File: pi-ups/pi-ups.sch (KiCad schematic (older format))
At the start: 34 parts, among them J1 , Q1 IRLML2244, Q2 IRLML2244, Q3 IRLML2244, Q4 IRLML2244, U1 BMS_1S, U2 DC-DC, U3 BMS_1S, U4 FTDI232, U5 Arduino_Pro_Mini

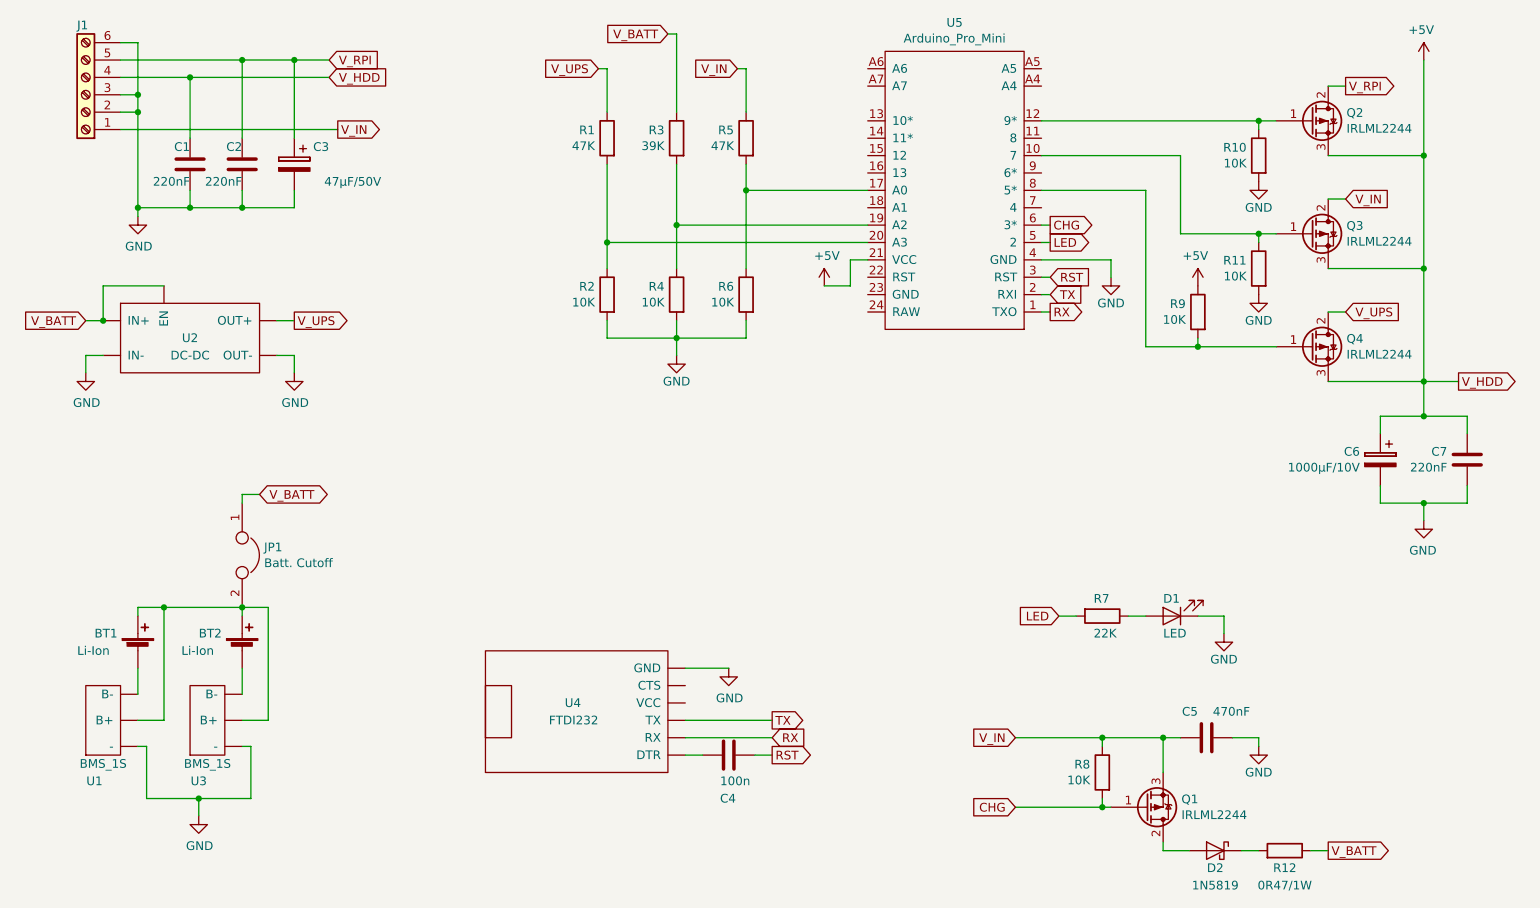
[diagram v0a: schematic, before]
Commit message: Update pi-ups.sch
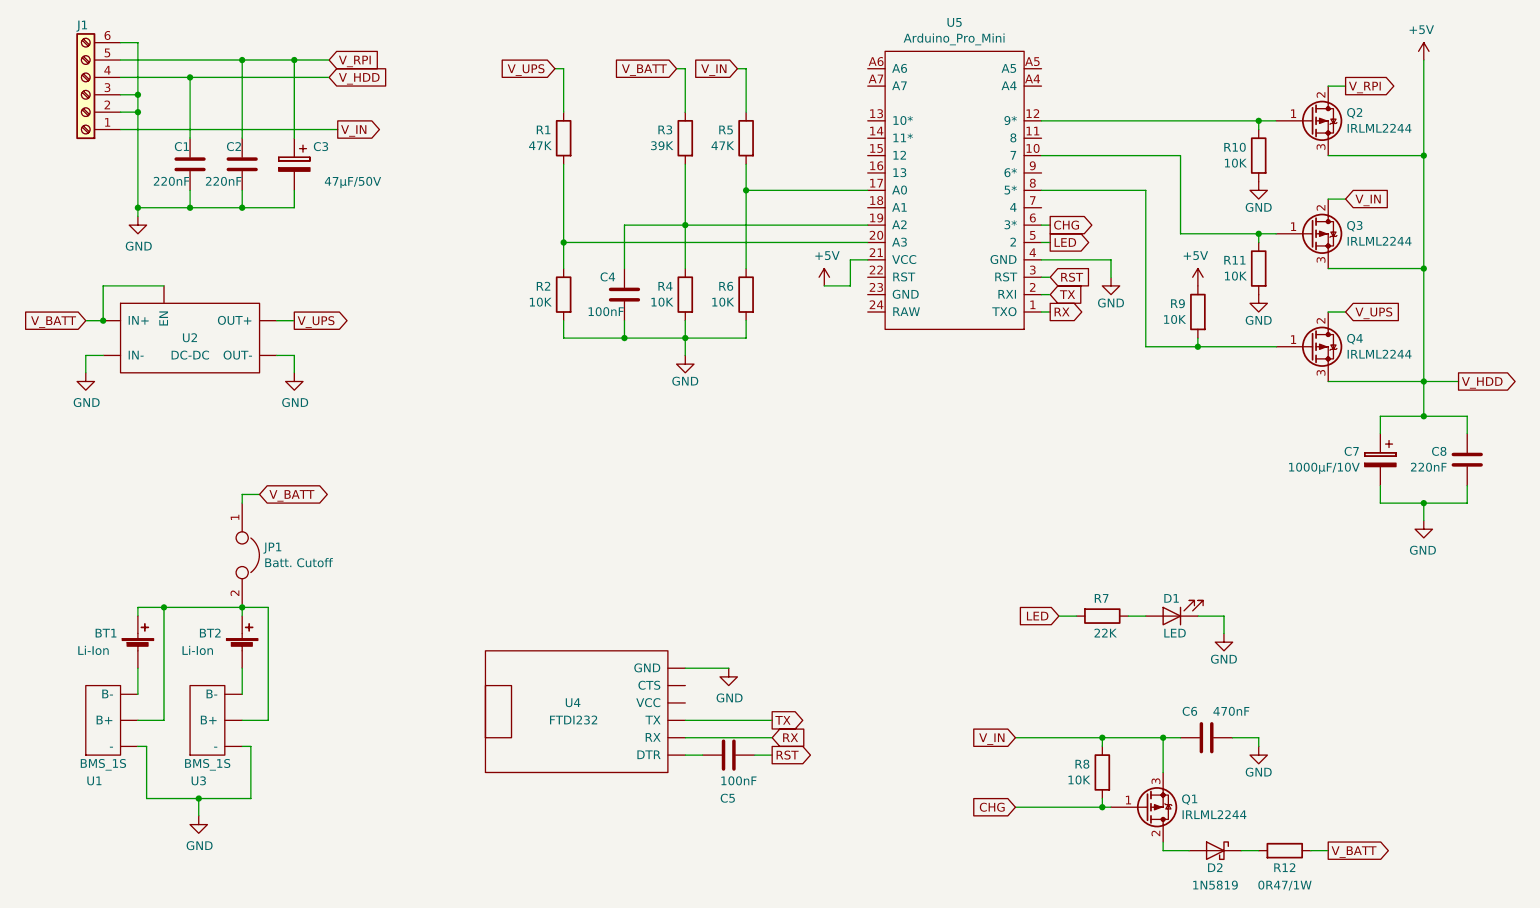
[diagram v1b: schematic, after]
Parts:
- added C4: 100nF, symbol Device:C
- C5: renamed from C4; value 100n -> 100nF
- renumbered C5 to C6, C6 to C7, C7 to C8
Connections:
- net GND: now also C4.2
- net at R3.2, R4.1, U5.19 (A2): now also C4.1
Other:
- moved on the sheet: R1, R2, R3, R4
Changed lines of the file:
@@
 $EndComp
 $Comp
-L Device:C C4
+L Device:C C5
 U 1 1 5CDDD4BF
 P 5700 5350
-F 0 "C4" V 5950 5400 50  0000 R CNN
-F 1 "100n" V 5850 5400 50  0000 R CNN
+F 0 "C5" V 5950 5400 50  0000 R CNN
+F 1 "100nF" V 5850 5400 50  0000 R CNN
 F 2 "" H 5738 5200 50  0001 C CNN
 F 3 "~" H 5700 5350 50  0001 C CNN
@@
 $EndComp
 $Comp
-L Device:CP C6
+L Device:CP C7
 U 1 1 5CE05AE7
 P 9450 3650
-F 0 "C6" H 9568 3696 50  0000 L CNN
+F 0 "C7" H 9568 3696 50  0000 L CNN
 F 1 "1000µF/10V" H 9568 3605 50  0000 L CNN
 F 2 "" H 9488 3500 50  0001 C CNN
@@
 $EndComp
 $Comp
-L Device:C C7
+L Device:C C8
 U 1 1 5CE05C0B
 P 9950 3650
-F 0 "C7" H 9835 3696 50  0000 R CNN
+F 0 "C8" H 9835 3696 50  0000 R CNN
 F 1 "220nF" H 9835 3605 50  0000 R CNN
 F 2 "" H 9988 3500 50  0001 C CNN
@@
 L Device:R R4
 U 1 1 5CE7E21F
-P 5400 2700
-F 0 "R4" H 5470 2746 50  0000 L CNN
-F 1 "10K" H 5470 2655 50  0000 L CNN
-F 2 "" V 5330 2700 50  0001 C CNN
-F 3 "~" H 5400 2700 50  0001 C CNN
-	1    5400 2700
+P 5450 2700
+F 0 "R4" H 5520 2746 50  0000 L CNN
+F 1 "10K" H 5520 2655 50  0000 L CNN
+F 2 "" V 5380 2700 50  0001 C CNN
+F 3 "~" H 5450 2700 50  0001 C CNN
+	1    5450 2700
 	-1   0    0    -1
 $EndComp
@@
 L Device:R R2
 U 1 1 5CE7E25D
-P 5000 2700
-F 0 "R2" H 5070 2746 50  0000 L CNN
-F 1 "10K" H 5070 2655 50  0000 L CNN
-F 2 "" V 4930 2700 50  0001 C CNN
-F 3 "~" H 5000 2700 50  0001 C CNN
-	1    5000 2700
+P 4750 2700
+F 0 "R2" H 4820 2746 50  0000 L CNN
+F 1 "10K" H 4820 2655 50  0000 L CNN
+F 2 "" V 4680 2700 50  0001 C CNN
+F 3 "~" H 4750 2700 50  0001 C CNN
+	1    4750 2700
 	-1   0    0    -1
 $EndComp
@@
 	5800 2850 5800 2950
 Wire Wire Line
-	5800 2950 5400 2950
-Wire Wire Line
-	5000 2950 5000 2850
+	4750 2950 4750 2850
 $Comp
 L power:GND #PWR05
 U 1 1 5CE8025B
-P 5400 3050
-F 0 "#PWR05" H 5400 2800 50  0001 C CNN
-F 1 "GND" H 5400 2900 50  0000 C CNN
-F 2 "" H 5400 3050 50  0001 C CNN
-F 3 "" H 5400 3050 50  0001 C CNN
-	1    5400 3050
-	-1   0    0    -1
-$EndComp
-Wire Wire Line
-	5400 3050 5400 2950
-Connection ~ 5400 2950
-Wire Wire Line
-	5400 2950 5000 2950
-Wire Wire Line
-	5400 2850 5400 2950
+P 5450 3050
+F 0 "#PWR05" H 5450 2800 50  0001 C CNN
+F 1 "GND" H 5450 2900 50  0000 C CNN
+F 2 "" H 5450 3050 50  0001 C CNN
+F 3 "" H 5450 3050 50  0001 C CNN
+	1    5450 3050
+	-1   0    0    -1
+$EndComp
+Wire Wire Line
+	5450 3050 5450 2950
+Connection ~ 5450 2950
+Wire Wire Line
+	5450 2950 5100 2950
+Wire Wire Line
+	5450 2850 5450 2950
 $Comp
 L Device:R R5
@@
 L Device:R R3
 U 1 1 5CE8442D
-P 5400 1800
-F 0 "R3" H 5470 1846 50  0000 L CNN
-F 1 "39K" H 5470 1755 50  0000 L CNN
-F 2 "" V 5330 1800 50  0001 C CNN
-F 3 "~" H 5400 1800 50  0001 C CNN
-	1    5400 1800
+P 5450 1800
+F 0 "R3" H 5520 1846 50  0000 L CNN
+F 1 "39K" H 5520 1755 50  0000 L CNN
+F 2 "" V 5380 1800 50  0001 C CNN
+F 3 "~" H 5450 1800 50  0001 C CNN
+	1    5450 1800
 	-1   0    0    -1
 $EndComp
@@
 L Device:R R1
 U 1 1 5CE84472
-P 5000 1800
-F 0 "R1" H 5070 1846 50  0000 L CNN
-F 1 "47K" H 5070 1755 50  0000 L CNN
-F 2 "" V 4930 1800 50  0001 C CNN
-F 3 "~" H 5000 1800 50  0001 C CNN
-	1    5000 1800
+P 4750 1800
+F 0 "R1" H 4820 1846 50  0000 L CNN
+F 1 "47K" H 4820 1755 50  0000 L CNN
+F 2 "" V 4680 1800 50  0001 C CNN
+F 3 "~" H 4750 1800 50  0001 C CNN
+	1    4750 1800
 	-1   0    0    -1
 $EndComp
@@
 Wire Wire Line
 	5800 1400 5800 1650
-Text GLabel 4950 1400 0    50   Input ~ 0
+Text GLabel 4700 1400 0    50   Input ~ 0
 V_UPS
 Wire Wire Line
-	5000 1650 5000 1400
-Wire Wire Line
-	5000 1400 4950 1400
+	4750 1650 4750 1400
+Wire Wire Line
+	4750 1400 4700 1400
 Text GLabel 7550 2400 2    50   Output ~ 0
 LED
@@
 	5800 1950 5800 2100
 Wire Wire Line
-	5400 1950 5400 2300
-Wire Wire Line
-	5000 1950 5000 2400
+	5450 1950 5450 2300
+Wire Wire Line
+	4750 1950 4750 2400
 Wire Wire Line
 	6500 2100 5800 2100
@@
 Wire Wire Line
 	5800 2100 5800 2550
-Wire Wire Line
-	6500 2300 5400 2300
-Connection ~ 5400 2300
-Wire Wire Line
-	5400 2300 5400 2550
-Wire Wire Line
-	6500 2400 5000 2400
-Connection ~ 5000 2400
-Wire Wire Line
-	5000 2400 5000 2550
+Connection ~ 5450 2300
+Connection ~ 4750 2400
+Wire Wire Line
+	4750 2400 4750 2550
 Wire Wire Line
 	8300 1900 8300 2350
@@
 Text GLabel 9150 5900 2    50   Output ~ 0
 V_BATT
-Text GLabel 5350 1200 0    50   Input ~ 0
+Text GLabel 5400 1400 0    50   Input ~ 0
 V_BATT
 Wire Wire Line
-	5350 1200 5400 1200
-Wire Wire Line
-	5400 1200 5400 1650
+	5400 1400 5450 1400
+Wire Wire Line
+	5450 1400 5450 1650
 Text GLabel 9900 3200 2    50   Output ~ 0
 V_HDD
@@
 	2200 1450 2600 1450
 $Comp
-L Device:C C5
+L Device:C C6
 U 1 1 5CEA3D6D
 P 8450 5250
-F 0 "C5" V 8300 5200 50  0000 R CNN
+F 0 "C6" V 8300 5200 50  0000 R CNN
 F 1 "470nF" V 8300 5500 50  0000 R CNN
 F 2 "" H 8488 5100 50  0001 C CNN
@@
 Wire Wire Line
 	3200 1350 3400 1350
+$Comp
+L Device:C C4
+U 1 1 5CF4324E
+P 5100 2700
+F 0 "C4" H 5050 2800 50  0000 R CNN
+F 1 "100nF" H 5100 2600 50  0000 R CNN
+F 2 "" H 5138 2550 50  0001 C CNN
+F 3 "~" H 5100 2700 50  0001 C CNN
+	1    5100 2700
+	1    0    0    -1
+$EndComp
+Wire Wire Line
+	4750 2400 6500 2400
+Wire Wire Line
+	5450 2950 5800 2950
+Wire Wire Line
+	5450 2300 6500 2300
+Wire Wire Line
+	5100 2950 5100 2850
+Connection ~ 5100 2950
+Wire Wire Line
+	5100 2950 4750 2950
+Wire Wire Line
+	5450 2300 5450 2550
+Wire Wire Line
+	5100 2300 5450 2300
+Wire Wire Line
+	5100 2300 5100 2550
 $EndSCHEMATC

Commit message: Update pi-ups.sch
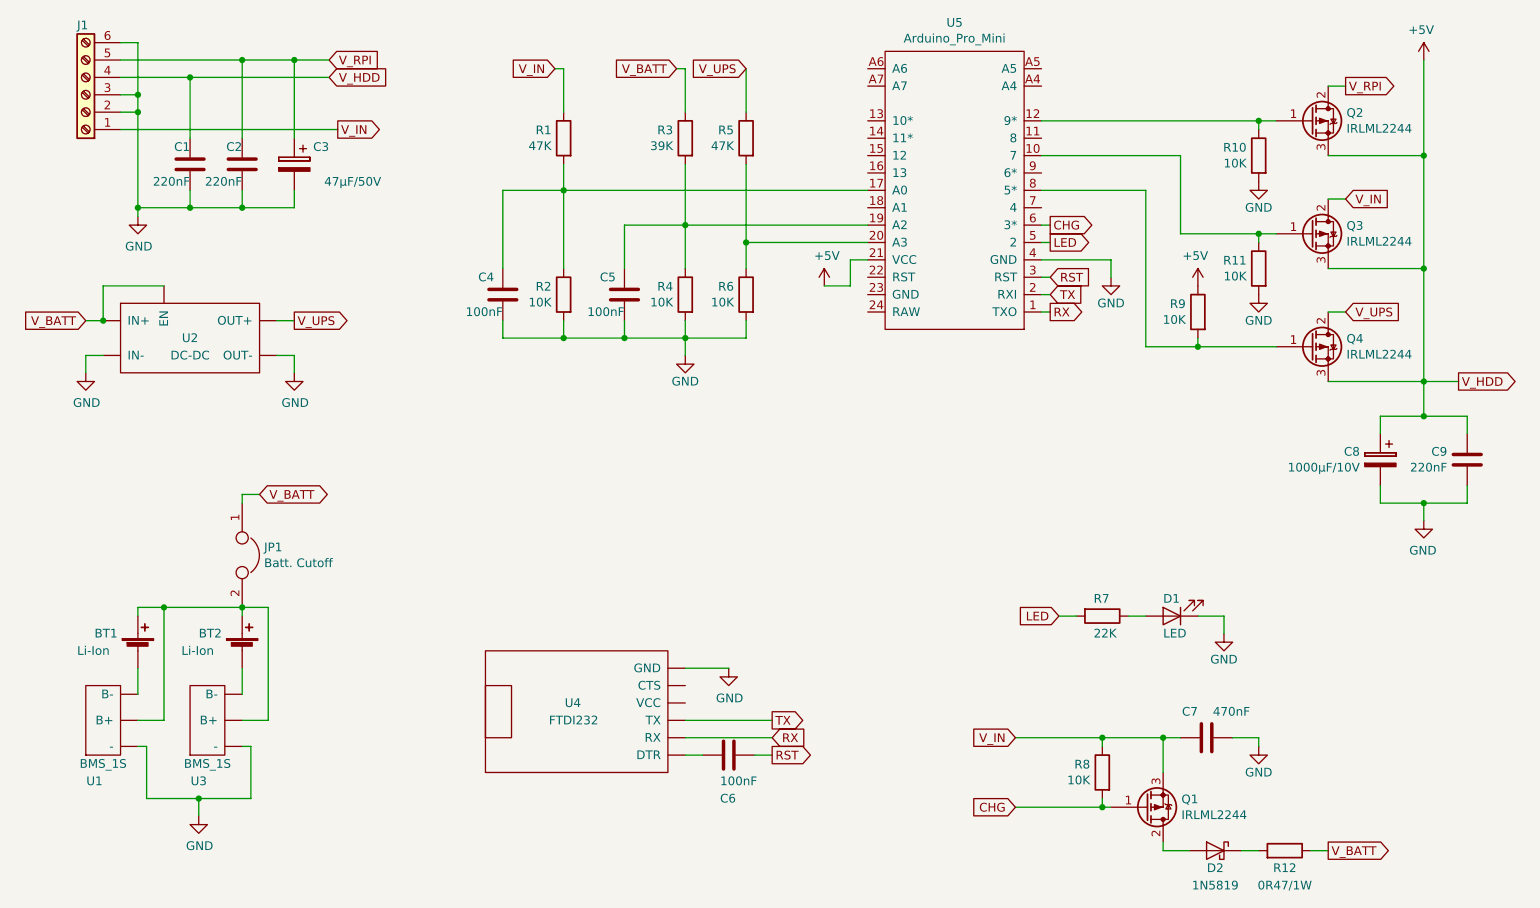
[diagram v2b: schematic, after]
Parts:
- added C4: 100nF, symbol Device:C
- renumbered C4 to C5, C5 to C6, C6 to C7, C7 to C8, C8 to C9
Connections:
- net GND: now also C4.2
- net V_IN: now also R1.1; no longer R5.1
- net V_UPS: now also R5.1; no longer R1.1
- net at R5.2, R6.1: now also U5.20 (A3); no longer U5.17 (A0)
- net at R1.2, R2.1: now also U5.17 (A0), C4.1; no longer U5.20 (A3)
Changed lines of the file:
@@
 $EndComp
 $Comp
-L Device:C C5
+L Device:C C6
 U 1 1 5CDDD4BF
 P 5700 5350
-F 0 "C5" V 5950 5400 50  0000 R CNN
+F 0 "C6" V 5950 5400 50  0000 R CNN
 F 1 "100nF" V 5850 5400 50  0000 R CNN
 F 2 "" H 5738 5200 50  0001 C CNN
@@
 $EndComp
 $Comp
-L Device:CP C7
+L Device:CP C8
 U 1 1 5CE05AE7
 P 9450 3650
-F 0 "C7" H 9568 3696 50  0000 L CNN
+F 0 "C8" H 9568 3696 50  0000 L CNN
 F 1 "1000µF/10V" H 9568 3605 50  0000 L CNN
 F 2 "" H 9488 3500 50  0001 C CNN
@@
 $EndComp
 $Comp
-L Device:C C8
+L Device:C C9
 U 1 1 5CE05C0B
 P 9950 3650
-F 0 "C8" H 9835 3696 50  0000 R CNN
+F 0 "C9" H 9835 3696 50  0000 R CNN
 F 1 "220nF" H 9835 3605 50  0000 R CNN
 F 2 "" H 9988 3500 50  0001 C CNN
@@
 	-1   0    0    -1
 $EndComp
-Text GLabel 5750 1400 0    50   Input ~ 0
+Text GLabel 4700 1400 0    50   Input ~ 0
 V_IN
 Wire Wire Line
-	5750 1400 5800 1400
-Wire Wire Line
 	5800 1400 5800 1650
-Text GLabel 4700 1400 0    50   Input ~ 0
+Text GLabel 5800 1400 0    50   Input ~ 0
 V_UPS
 Wire Wire Line
@@
 	7900 2500 7900 2600
 Wire Wire Line
-	5800 1950 5800 2100
-Wire Wire Line
 	5450 1950 5450 2300
-Wire Wire Line
-	4750 1950 4750 2400
-Wire Wire Line
-	6500 2100 5800 2100
-Connection ~ 5800 2100
-Wire Wire Line
-	5800 2100 5800 2550
 Connection ~ 5450 2300
-Connection ~ 4750 2400
-Wire Wire Line
-	4750 2400 4750 2550
 Wire Wire Line
 	8300 1900 8300 2350
@@
 	2200 1450 2600 1450
 $Comp
-L Device:C C6
+L Device:C C7
 U 1 1 5CEA3D6D
 P 8450 5250
-F 0 "C6" V 8300 5200 50  0000 R CNN
+F 0 "C7" V 8300 5200 50  0000 R CNN
 F 1 "470nF" V 8300 5500 50  0000 R CNN
 F 2 "" H 8488 5100 50  0001 C CNN
@@
 	3200 1350 3400 1350
 $Comp
-L Device:C C4
+L Device:C C5
 U 1 1 5CF4324E
 P 5100 2700
-F 0 "C4" H 5050 2800 50  0000 R CNN
+F 0 "C5" H 5050 2800 50  0000 R CNN
 F 1 "100nF" H 5100 2600 50  0000 R CNN
 F 2 "" H 5138 2550 50  0001 C CNN
@@
 $EndComp
 Wire Wire Line
-	4750 2400 6500 2400
-Wire Wire Line
 	5450 2950 5800 2950
 Wire Wire Line
@@
 Wire Wire Line
 	5100 2300 5100 2550
+Wire Wire Line
+	4750 1950 4750 2100
+Wire Wire Line
+	6500 2400 5800 2400
+Connection ~ 5800 2400
+Wire Wire Line
+	5800 2400 5800 2550
+Wire Wire Line
+	5800 1950 5800 2400
+Wire Wire Line
+	6500 2100 4750 2100
+Connection ~ 4750 2100
+Wire Wire Line
+	4750 2100 4750 2550
+$Comp
+L Device:C C4
+U 1 1 5D02415F
+P 4400 2700
+F 0 "C4" H 4350 2800 50  0000 R CNN
+F 1 "100nF" H 4400 2600 50  0000 R CNN
+F 2 "" H 4438 2550 50  0001 C CNN
+F 3 "~" H 4400 2700 50  0001 C CNN
+	1    4400 2700
+	1    0    0    -1
+$EndComp
+Wire Wire Line
+	4400 2850 4400 2950
+Wire Wire Line
+	4400 2950 4750 2950
+Connection ~ 4750 2950
+Wire Wire Line
+	4400 2550 4400 2100
+Wire Wire Line
+	4400 2100 4750 2100
 $EndSCHEMATC

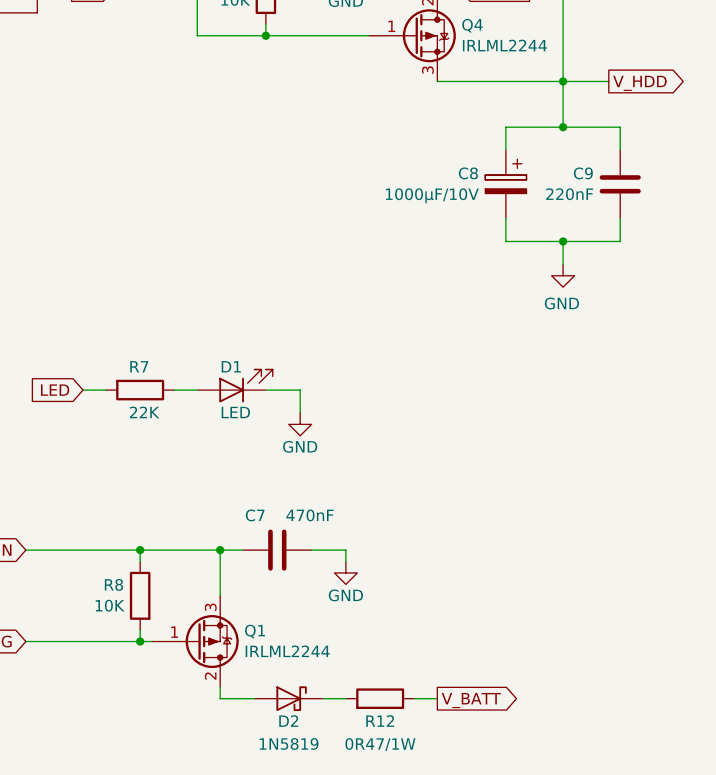
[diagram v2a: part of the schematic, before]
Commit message: Update pi-ups.sch
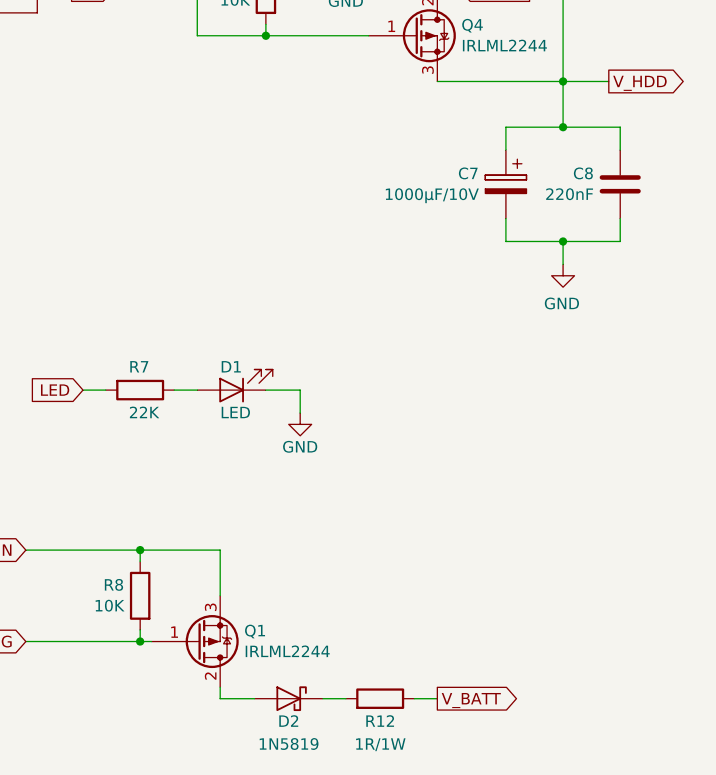
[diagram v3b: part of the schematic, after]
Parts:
- removed C7: 470nF, symbol Device:C
- R12: value 0R47/1W -> 1R/1W
- renumbered C8 to C7, C9 to C8
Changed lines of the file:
@@
 $EndComp
 $Comp
-L power:+5V #PWR014
+L power:+5V #PWR013
 U 1 1 5CDF6DD4
 P 9700 1350
-F 0 "#PWR014" H 9700 1200 50  0001 C CNN
+F 0 "#PWR013" H 9700 1200 50  0001 C CNN
 F 1 "+5V" H 9715 1523 50  0000 C CNN
 F 2 "" H 9700 1350 50  0001 C CNN
@@
 $EndComp
 $Comp
-L Device:CP C8
+L Device:CP C7
 U 1 1 5CE05AE7
 P 9450 3650
-F 0 "C8" H 9568 3696 50  0000 L CNN
+F 0 "C7" H 9568 3696 50  0000 L CNN
 F 1 "1000µF/10V" H 9568 3605 50  0000 L CNN
 F 2 "" H 9488 3500 50  0001 C CNN
@@
 $EndComp
 $Comp
-L Device:C C9
+L Device:C C8
 U 1 1 5CE05C0B
 P 9950 3650
-F 0 "C9" H 9835 3696 50  0000 R CNN
+F 0 "C8" H 9835 3696 50  0000 R CNN
 F 1 "220nF" H 9835 3605 50  0000 R CNN
 F 2 "" H 9988 3500 50  0001 C CNN
@@
 	9700 3200 9150 3200
 $Comp
-L power:GND #PWR015
+L power:GND #PWR014
 U 1 1 5CE0B0C6
 P 9700 4000
-F 0 "#PWR015" H 9700 3750 50  0001 C CNN
+F 0 "#PWR014" H 9700 3750 50  0001 C CNN
 F 1 "GND" H 9705 3827 50  0000 C CNN
 F 2 "" H 9700 4000 50  0001 C CNN
@@
 P 8900 5900
 F 0 "R12" V 8800 5900 50  0000 C CNN
-F 1 "0R47/1W" V 8700 5900 50  0000 C CNN
+F 1 "1R/1W" V 8700 5900 50  0000 C CNN
 F 2 "" V 8830 5900 50  0001 C CNN
 F 3 "~" H 8900 5900 50  0001 C CNN
@@
 	2200 1450 2600 1450
 $Comp
-L Device:C C7
-U 1 1 5CEA3D6D
-P 8450 5250
-F 0 "C7" V 8300 5200 50  0000 R CNN
-F 1 "470nF" V 8300 5500 50  0000 R CNN
-F 2 "" H 8488 5100 50  0001 C CNN
-F 3 "~" H 8450 5250 50  0001 C CNN
-	1    8450 5250
-	0    1    1    0
-$EndComp
-$Comp
 L Device:C C1
 U 1 1 5CEC0215
@@
 	7350 5650 7850 5650
 $Comp
-L power:GND #PWR013
-U 1 1 5CEF6310
-P 8750 5300
-F 0 "#PWR013" H 8750 5050 50  0001 C CNN
-F 1 "GND" H 8750 5150 50  0000 C CNN
-F 2 "" H 8750 5300 50  0001 C CNN
-F 3 "" H 8750 5300 50  0001 C CNN
-	1    8750 5300
-	1    0    0    -1
-$EndComp
-Wire Wire Line
-	8200 5250 8300 5250
-Connection ~ 8200 5250
-Wire Wire Line
-	8600 5250 8750 5250
-Wire Wire Line
-	8750 5250 8750 5300
-$Comp
 L Device:CP C3
